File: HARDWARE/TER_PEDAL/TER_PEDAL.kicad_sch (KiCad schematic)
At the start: 0 parts

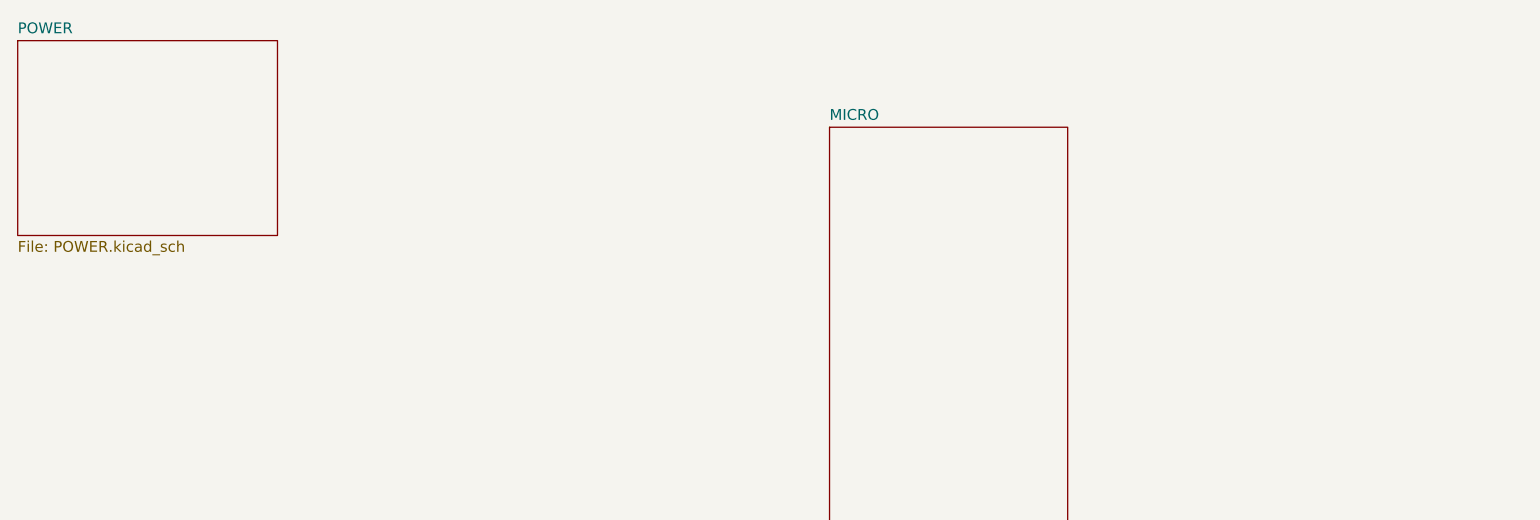
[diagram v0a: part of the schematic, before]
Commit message: Added Can transceiver Circuit
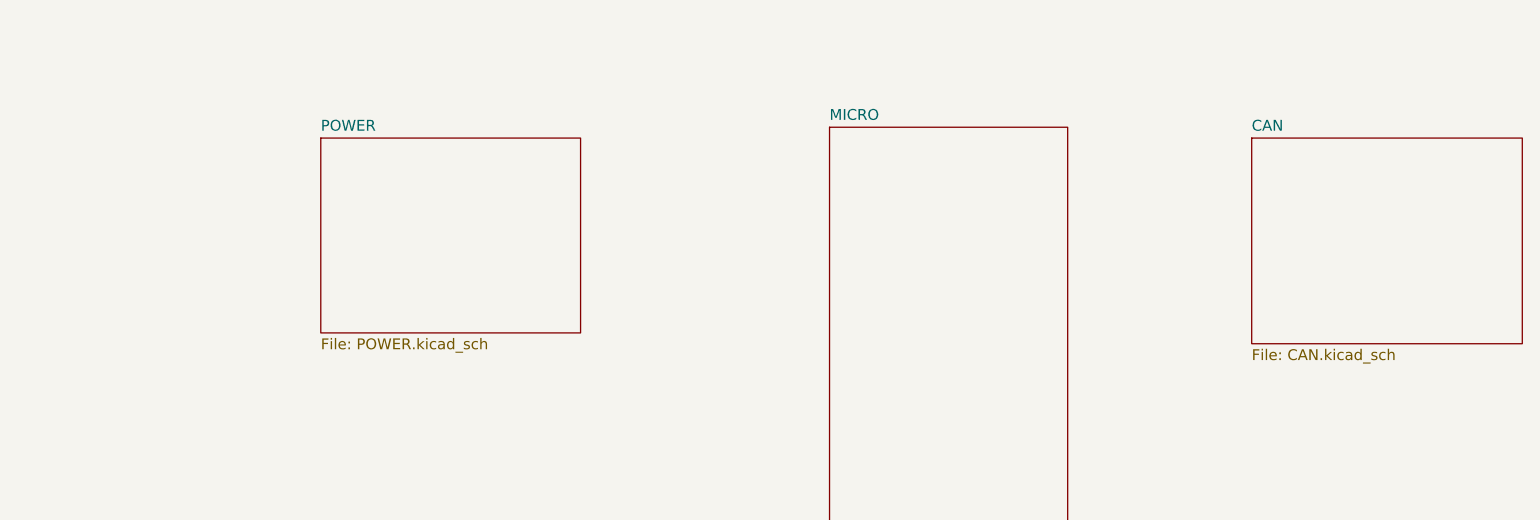
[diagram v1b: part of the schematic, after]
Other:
- added sheet CAN (CAN.kicad_sch)
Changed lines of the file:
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@@
 (kicad_sch (version 20230121) (generator eeschema)
   (paper "A4")
-  (sheet (at 26.67 25.4) (size 30.48 22.86) (fields_autoplaced)
+  (sheet (at 62.23 36.83) (size 30.48 22.86) (fields_autoplaced)
     (stroke (width 0.1524) (type solid))
     (fill (color 0 0 0 0.0000))
-    (property "Sheetname" "POWER" (at 26.67 24.6884 0)
+    (property "Sheetname" "POWER" (at 62.23 36.1184 0)
       (effects (font (size 1.27 1.27)) (justify left bottom))
     )
-    (property "Sheetfile" "POWER.kicad_sch" (at 26.67 48.8446 0)
+    (property "Sheetfile" "POWER.kicad_sch" (at 62.23 60.2746 0)
       (effects (font (size 1.27 1.27)) (justify left top))
     )
@@
       )
     )
+  )
+  (sheet (at 171.45 36.83) (size 31.75 24.13) (fields_autoplaced)
+    (stroke (width 0.1524) (type solid))
+    (fill (color 0 0 0 0.0000))
+    (property "Sheetname" "CAN" (at 171.45 36.1184 0)
+      (effects (font (size 1.27 1.27)) (justify left bottom))
+    )
+    (property "Sheetfile" "CAN.kicad_sch" (at 171.45 61.5446 0)
+      (effects (font (size 1.27 1.27)) (justify left top))
+    )
+    (instances
+      (project "TER_PEDAL"
+        (path "/73ede3a3-6344-40fe-9207-10ff50d388ba" (page "4"))
+      )
+    )

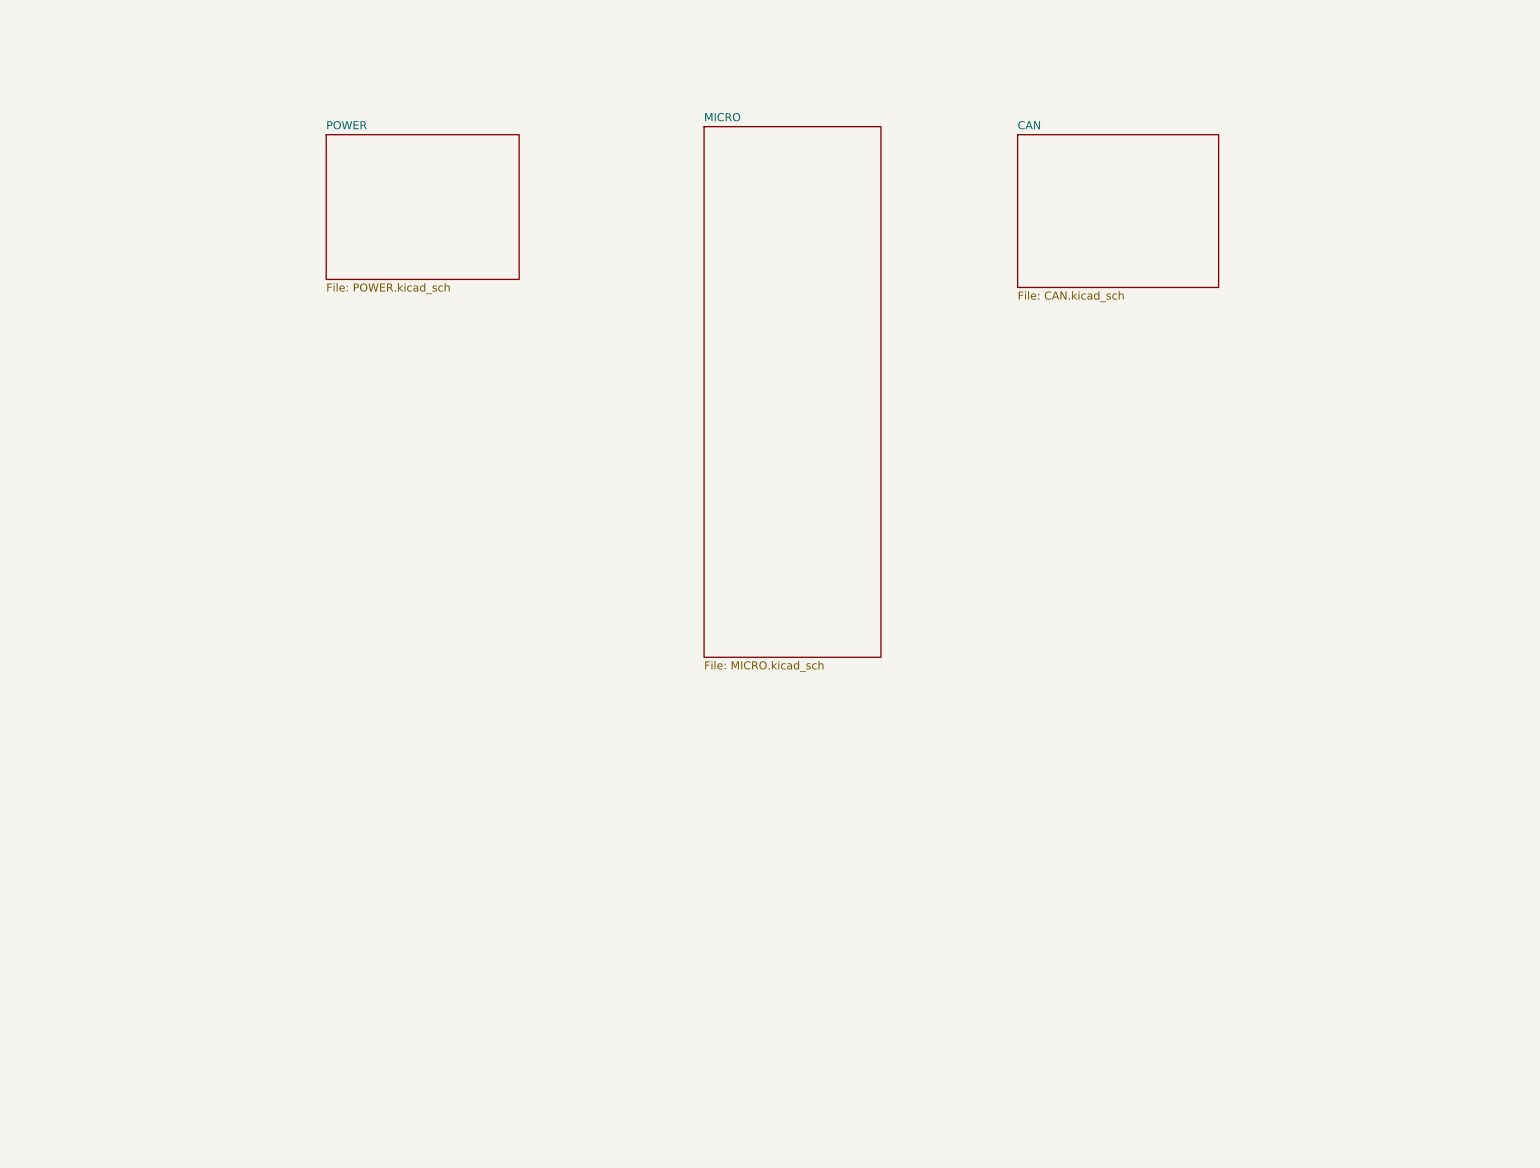
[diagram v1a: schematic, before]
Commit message: Added Uniport, Debug and began sensors design
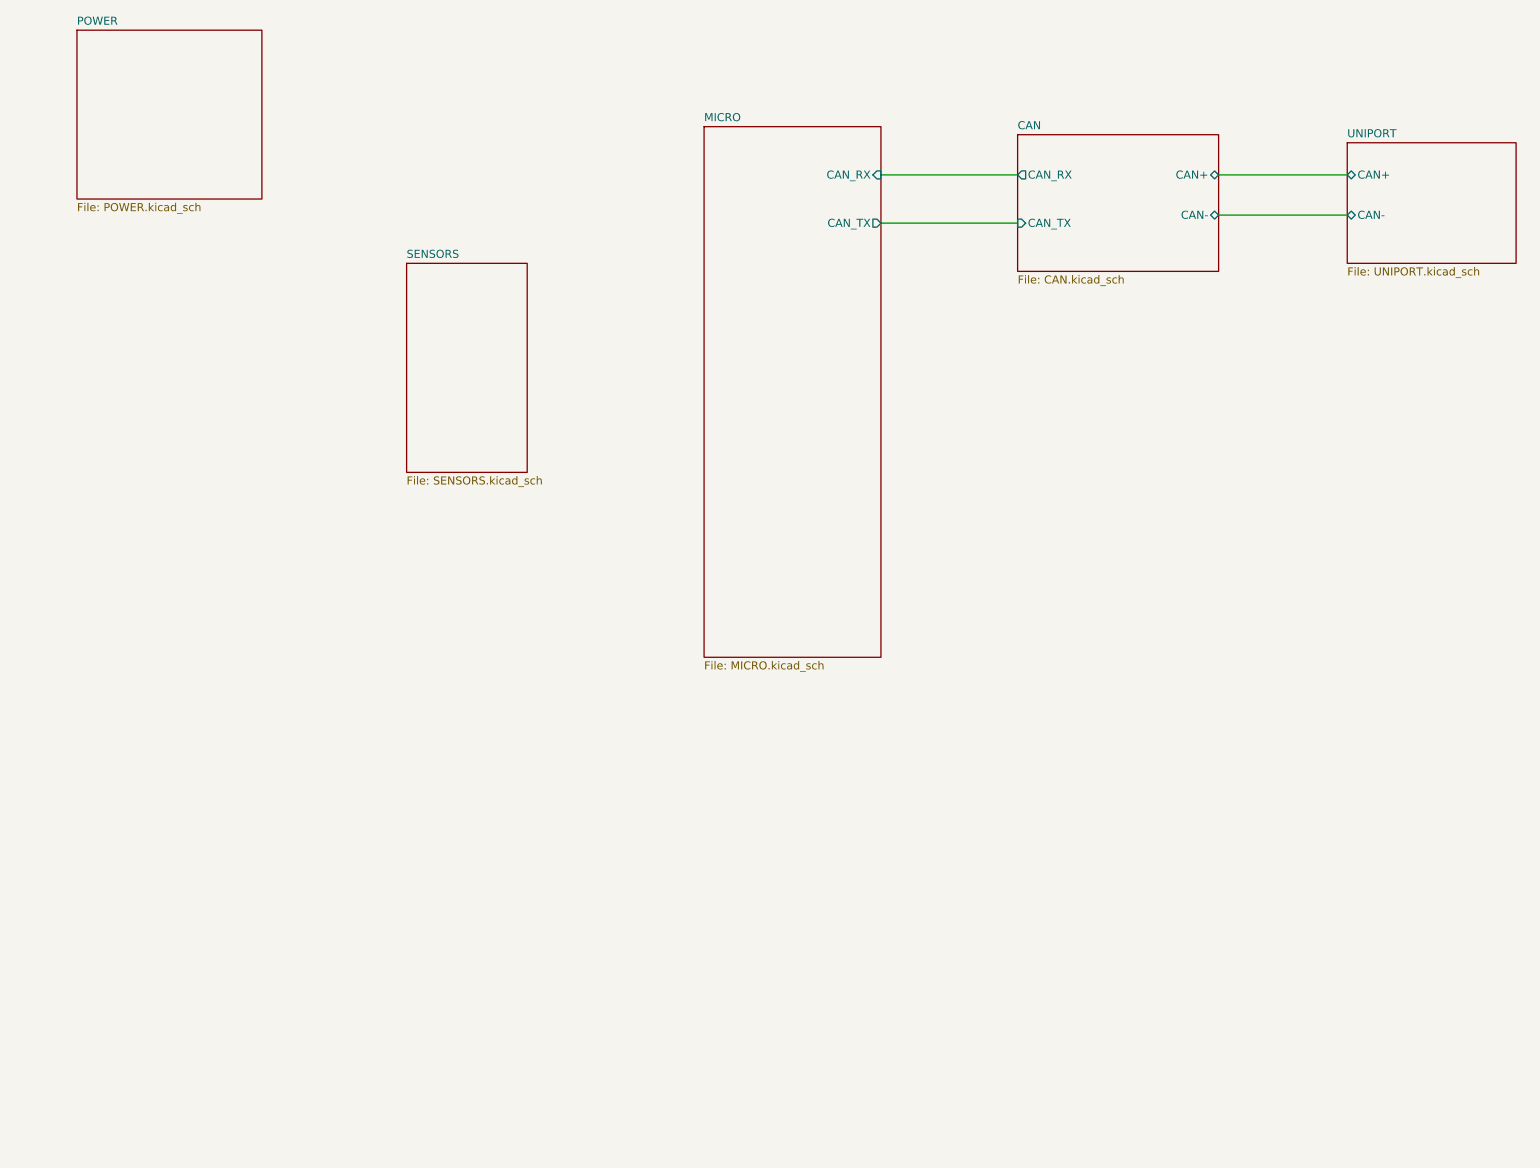
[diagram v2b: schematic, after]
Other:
- added sheet SENSORS (SENSORS.kicad_sch)
- added sheet UNIPORT (UNIPORT.kicad_sch)
- sheet CAN ports: added CAN+, CAN-, CAN_RX, CAN_TX; removed none
- sheet MICRO ports: added CAN_RX, CAN_TX; removed none
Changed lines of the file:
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@@
 (kicad_sch (version 20230121) (generator eeschema)
   (paper "A4")
-  (sheet (at 62.23 36.83) (size 30.48 22.86) (fields_autoplaced)
+  (wire (pts (xy 203.2 49.53) (xy 223.52 49.53))
+    (stroke (width 0) (type default))
+  )
+  (wire (pts (xy 149.86 43.18) (xy 171.45 43.18))
+    (stroke (width 0) (type default))
+  )
+  (wire (pts (xy 203.2 43.18) (xy 223.52 43.18))
+    (stroke (width 0) (type default))
+  )
+  (wire (pts (xy 149.86 50.8) (xy 171.45 50.8))
+    (stroke (width 0) (type default))
+  )
+  (sheet (at 223.52 38.1) (size 26.67 19.05) (fields_autoplaced)
     (stroke (width 0.1524) (type solid))
     (fill (color 0 0 0 0.0000))
-    (property "Sheetname" "POWER" (at 62.23 36.1184 0)
+    (property "Sheetname" "UNIPORT" (at 223.52 37.3884 0)
       (effects (font (size 1.27 1.27)) (justify left bottom))
     )
-    (property "Sheetfile" "POWER.kicad_sch" (at 62.23 60.2746 0)
+    (property "Sheetfile" "UNIPORT.kicad_sch" (at 223.52 57.7346 0)
+      (effects (font (size 1.27 1.27)) (justify left top))
+    )
+    (pin "CAN+" bidirectional (at 223.52 43.18 180)
+      (effects (font (size 1.27 1.27)) (justify left))
+    )
+    (pin "CAN-" bidirectional (at 223.52 49.53 180)
+      (effects (font (size 1.27 1.27)) (justify left))
+    )
+    (instances
+      (project "TER_PEDAL"
+        (path "/73ede3a3-6344-40fe-9207-10ff50d388ba" (page "5"))
+      )
+    )
+  )
+  (sheet (at 22.86 20.32) (size 29.21 26.67) (fields_autoplaced)
+    (stroke (width 0.1524) (type solid))
+    (fill (color 0 0 0 0.0000))
+    (property "Sheetname" "POWER" (at 22.86 19.6084 0)
+      (effects (font (size 1.27 1.27)) (justify left bottom))
+    )
+    (property "Sheetfile" "POWER.kicad_sch" (at 22.86 47.5746 0)
       (effects (font (size 1.27 1.27)) (justify left top))
     )
@@
       (effects (font (size 1.27 1.27)) (justify left top))
     )
+    (pin "CAN_RX" input (at 149.86 43.18 0)
+      (effects (font (size 1.27 1.27)) (justify right))
+    )
+    (pin "CAN_TX" output (at 149.86 50.8 0)
+      (effects (font (size 1.27 1.27)) (justify right))
+    )
     (instances
       (project "TER_PEDAL"
@@
     )
   )
-  (sheet (at 171.45 36.83) (size 31.75 24.13) (fields_autoplaced)
+  (sheet (at 171.45 36.83) (size 31.75 21.59) (fields_autoplaced)
     (stroke (width 0.1524) (type solid))
     (fill (color 0 0 0 0.0000))
@@
       (effects (font (size 1.27 1.27)) (justify left bottom))
     )
-    (property "Sheetfile" "CAN.kicad_sch" (at 171.45 61.5446 0)
+    (property "Sheetfile" "CAN.kicad_sch" (at 171.45 59.0046 0)
       (effects (font (size 1.27 1.27)) (justify left top))
+    )
+    (pin "CAN_RX" output (at 171.45 43.18 180)
+      (effects (font (size 1.27 1.27)) (justify left))
+    )
+    (pin "CAN_TX" input (at 171.45 50.8 180)
+      (effects (font (size 1.27 1.27)) (justify left))
+    )
+    (pin "CAN+" bidirectional (at 203.2 43.18 0)
+      (effects (font (size 1.27 1.27)) (justify right))
+    )
+    (pin "CAN-" bidirectional (at 203.2 49.53 0)
+      (effects (font (size 1.27 1.27)) (justify right))
     )
     (instances
@@
       )
     )
+  )
+  (sheet (at 74.93 57.15) (size 19.05 33.02) (fields_autoplaced)
+    (stroke (width 0.1524) (type solid))
+    (fill (color 0 0 0 0.0000))
+    (property "Sheetname" "SENSORS" (at 74.93 56.4384 0)
+      (effects (font (size 1.27 1.27)) (justify left bottom))
+    )
+    (property "Sheetfile" "SENSORS.kicad_sch" (at 74.93 90.7546 0)
+      (effects (font (size 1.27 1.27)) (justify left top))
+    )
+    (instances
+      (project "TER_PEDAL"
+        (path "/73ede3a3-6344-40fe-9207-10ff50d388ba" (page "6"))
+      )
+    )

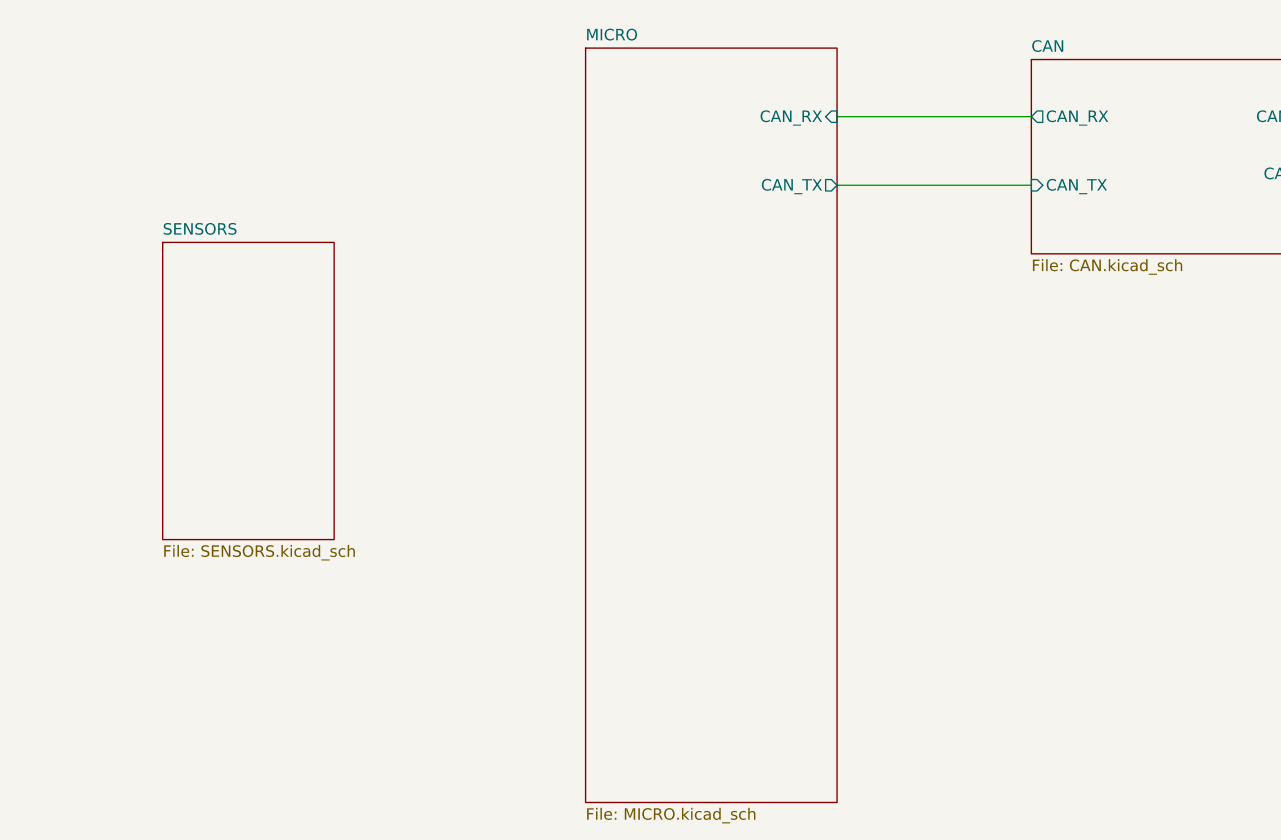
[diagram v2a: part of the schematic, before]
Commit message: Added footprints to existing components
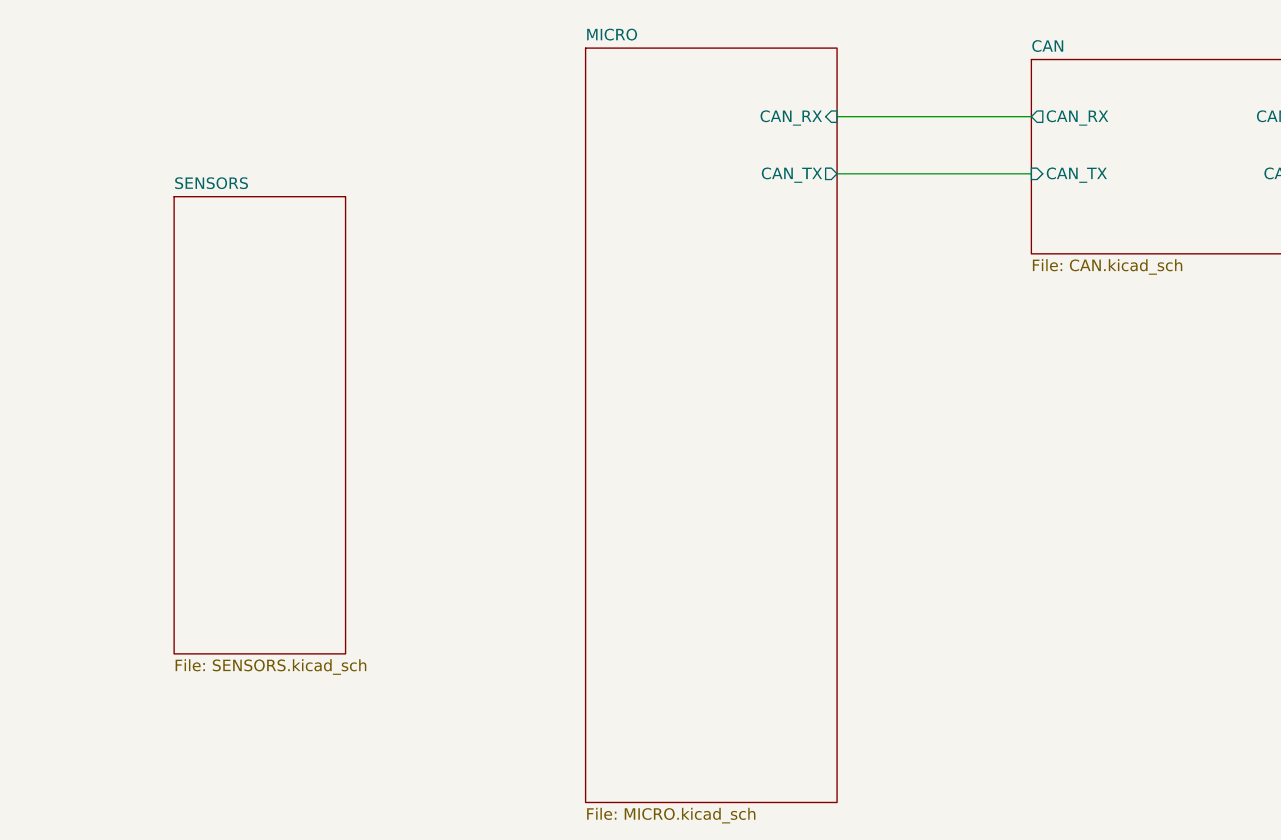
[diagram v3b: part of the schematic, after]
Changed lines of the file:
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@@
     (stroke (width 0) (type default))
   )
-  (wire (pts (xy 149.86 50.8) (xy 171.45 50.8))
+  (wire (pts (xy 149.86 49.53) (xy 171.45 49.53))
     (stroke (width 0) (type default))
   )
@@
       (effects (font (size 1.27 1.27)) (justify right))
     )
-    (pin "CAN_TX" output (at 149.86 50.8 0)
+    (pin "CAN_TX" output (at 149.86 49.53 0)
       (effects (font (size 1.27 1.27)) (justify right))
     )
@@
       (effects (font (size 1.27 1.27)) (justify left))
     )
-    (pin "CAN_TX" input (at 171.45 50.8 180)
+    (pin "CAN_TX" input (at 171.45 49.53 180)
       (effects (font (size 1.27 1.27)) (justify left))
     )
@@
     )
   )
-  (sheet (at 74.93 57.15) (size 19.05 33.02) (fields_autoplaced)
+  (sheet (at 76.2 52.07) (size 19.05 50.8) (fields_autoplaced)
     (stroke (width 0.1524) (type solid))
     (fill (color 0 0 0 0.0000))
-    (property "Sheetname" "SENSORS" (at 74.93 56.4384 0)
+    (property "Sheetname" "SENSORS" (at 76.2 51.3584 0)
       (effects (font (size 1.27 1.27)) (justify left bottom))
     )
-    (property "Sheetfile" "SENSORS.kicad_sch" (at 74.93 90.7546 0)
+    (property "Sheetfile" "SENSORS.kicad_sch" (at 76.2 103.4546 0)
       (effects (font (size 1.27 1.27)) (justify left top))
     )

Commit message: Finished Initial Schematic
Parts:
- added D3, D4, D5: LED, LED_SMD:LED_0603_1608Metric, symbol Device:LED
- added R13, R14: 120R, Resistor_SMD:R_0603_1608Metric, symbol Device:R
- added R15: 120R, Capacitor_SMD:C_0603_1608Metric, symbol Device:R
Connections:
- new net: D3.2 (A), R13.1
- new net: D5.2 (A), R15.1
- new net: D4.2 (A), R14.1
- new net +3.3V: R15.2
- new net DBG_LED: R13.2
- new net GND: D3.1 (K), D4.1 (K), D5.1 (K)
- new net IMP_LED: R14.2
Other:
- sheet MICRO ports: added APPS_1_ADC, APPS_2_ADC, BPPS_ADC, DBG_LED, IMP_LED; removed none
- sheet SENSORS ports: added APPS_1, APPS_2, BPPS; removed none
- note added: "STATUS LEDS"
